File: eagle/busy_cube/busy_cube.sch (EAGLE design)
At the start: 6 parts

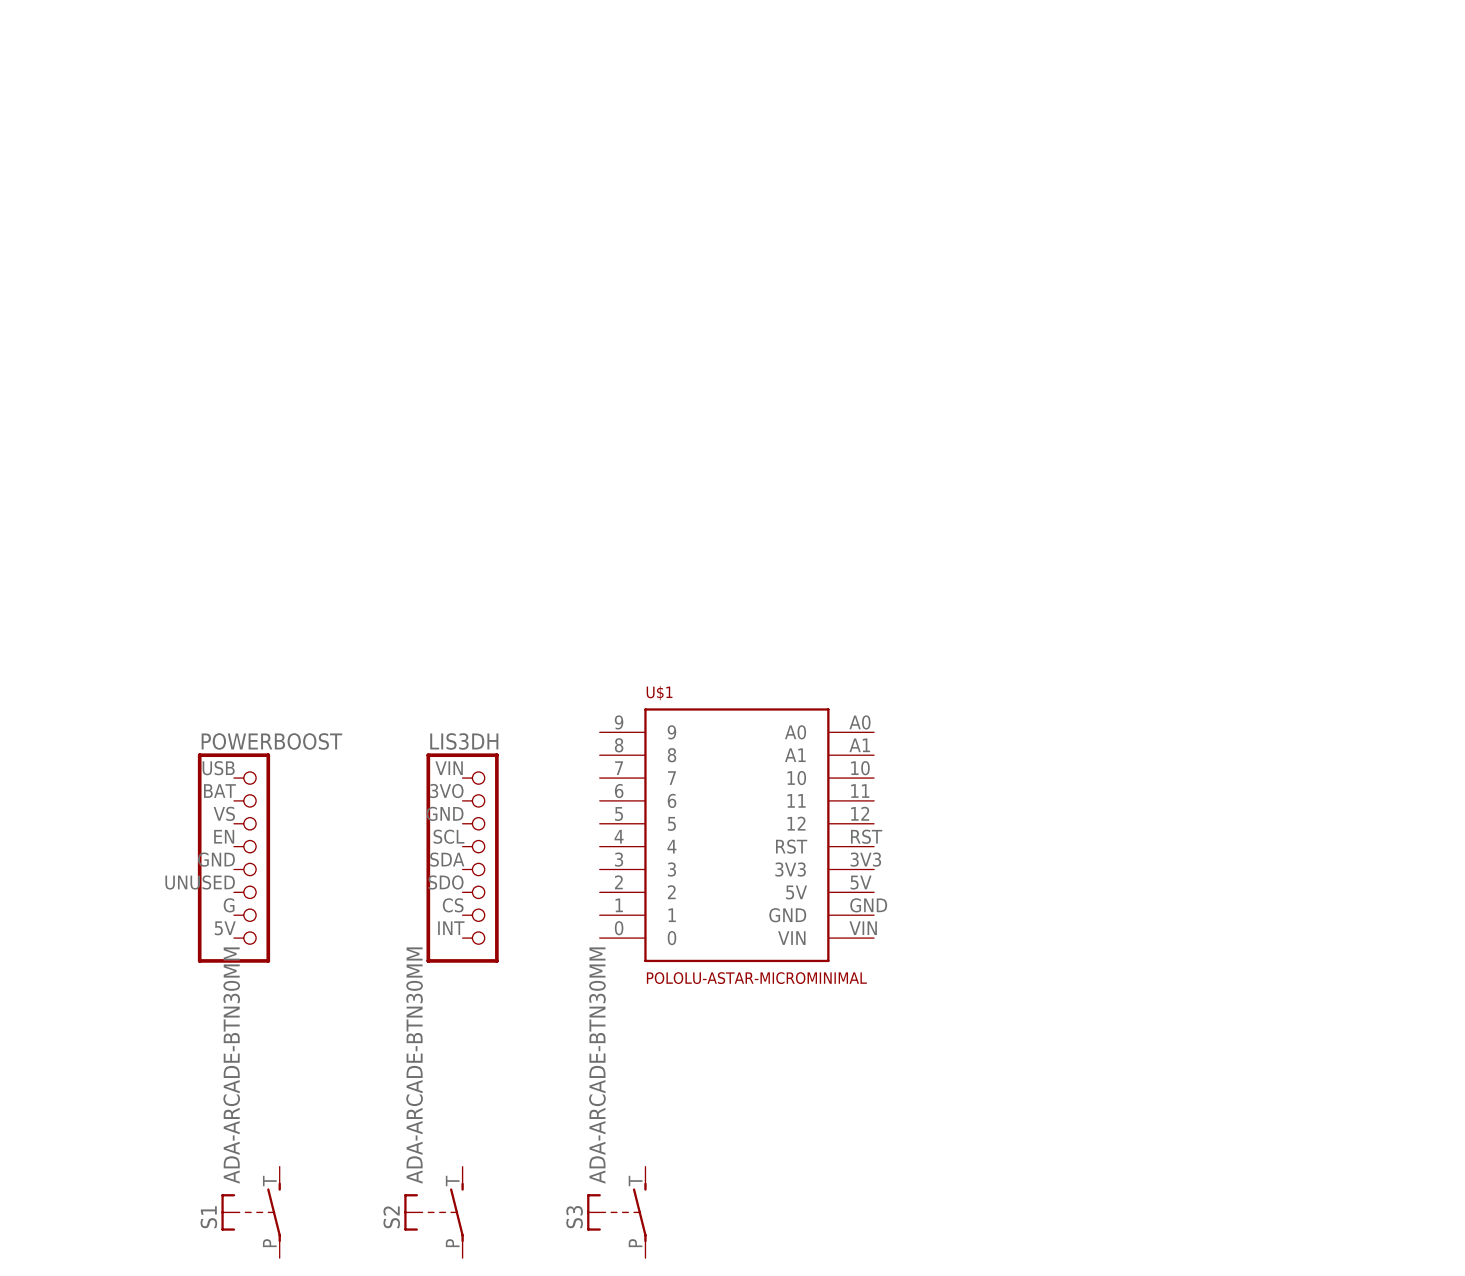
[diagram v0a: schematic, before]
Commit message: First attempt for wiring
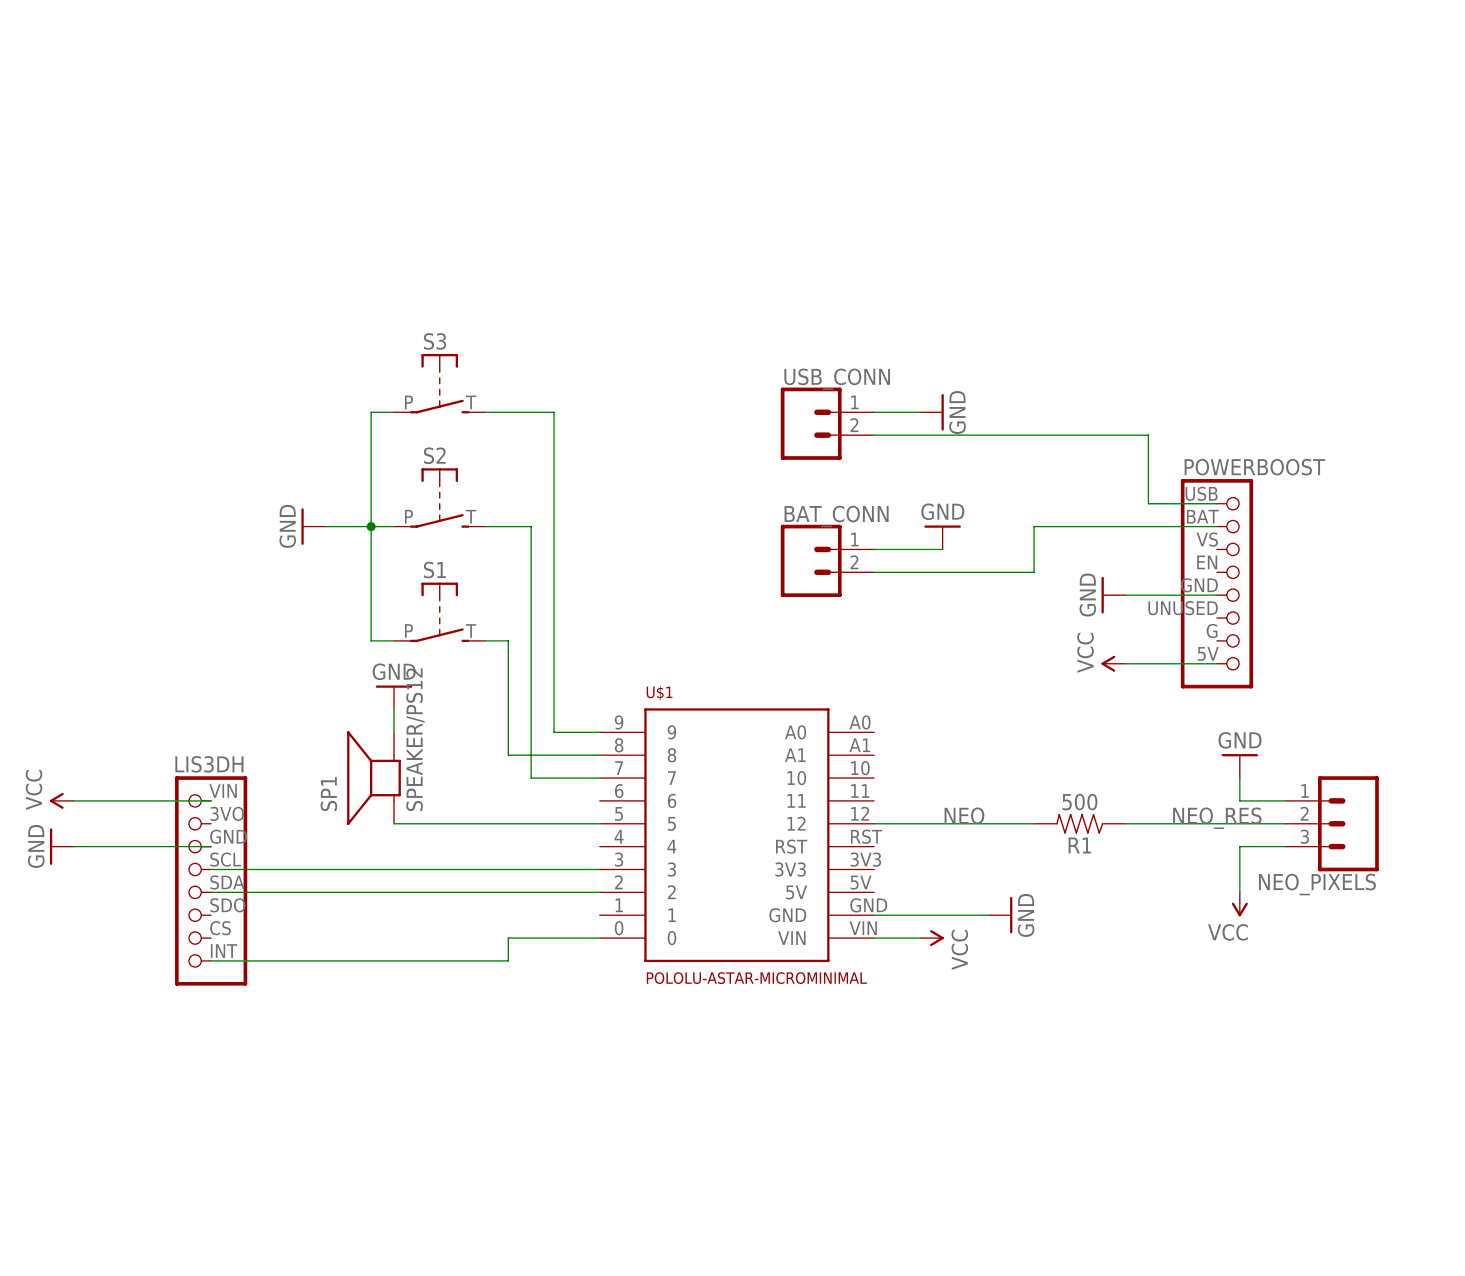
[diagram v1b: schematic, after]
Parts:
- added BAT_CONN, USB_CONN: (no value), busy_cube_lib:CONN_02-JST-2MM-SMT
- added NEO_PIXELS: (no value), busy_cube_lib:CONN_03LONGPADS
- added R1: 500, busy_cube_lib:RESISTORAXIAL-0.3
- added SP1: SPEAKER/PS12, busy_cube_lib:SPEAKER/PS12
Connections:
- new net BAT_IN_VCC: BAT_CONN.1, POWERBOOST.3VO
- new net BTN1: S1.S, U$1.8
- new net BTN2: S2.S, U$1.7
- new net BTN3: S3.S, U$1.9
- new net GND: BAT_CONN.2, LIS3DH.GND, NEO_PIXELS.1, POWERBOOST.SDA, S1.P, S2.P, S3.P, SP1.-, U$1.GND, USB_CONN.2
- new net N$1: LIS3DH.SCL, U$1.3
- new net N$2: LIS3DH.SDA, U$1.2
- new net N$3: LIS3DH.INT, U$1.0
- new net NEO: R1.2, U$1.12
- new net NEO_RES: NEO_PIXELS.2, R1.1
- new net SPKR: SP1.+, U$1.5
- new net USB_IN_VCC: POWERBOOST.VIN, USB_CONN.1
- new net VCC: LIS3DH.VIN, NEO_PIXELS.3, POWERBOOST.INT, U$1.VIN
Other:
- moved on the sheet: LIS3DH, POWERBOOST, S1, S2, S3

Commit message: some more changes
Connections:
- net BTN1: now also U$1.11; no longer U$1.8
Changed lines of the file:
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@@
-</segment>
-</net>
-<net name="BTN1" class="0">
-<segment>
-<pinref part="U$1" gate="G$1" pin="8"/>
-<wire x1="33.02" y1="66.04" x2="22.86" y2="66.04" width="0.1524" layer="91"/>
-<pinref part="S1" gate="G$1" pin="S"/>
-<wire x1="22.86" y1="78.74" x2="20.32" y2="78.74" width="0.1524" layer="91"/>
-<wire x1="22.86" y1="66.04" x2="22.86" y2="78.74" width="0.1524" layer="91"/>
 </segment>
 </net>
@@
 <pinref part="S3" gate="G$1" pin="S"/>
 <wire x1="27.94" y1="104.14" x2="20.32" y2="104.14" width="0.1524" layer="91"/>
+<label x="22.86" y="104.14" size="1.778" layer="95"/>
 </segment>
 </net>
@@
 <pinref part="U$1" gate="G$1" pin="7"/>
 <wire x1="25.4" y1="63.5" x2="33.02" y2="63.5" width="0.1524" layer="91"/>
+<label x="20.32" y="91.44" size="1.778" layer="95"/>
 </segment>
 </net>
@@
 </segment>
 </net>
+<net name="BTN1" class="0">
+<segment>
+<pinref part="S1" gate="G$1" pin="S"/>
+<wire x1="20.32" y1="78.74" x2="68.58" y2="78.74" width="0.1524" layer="91"/>
+<wire x1="68.58" y1="78.74" x2="68.58" y2="60.96" width="0.1524" layer="91"/>
+<pinref part="U$1" gate="G$1" pin="11"/>
+<wire x1="68.58" y1="60.96" x2="63.5" y2="60.96" width="0.1524" layer="91"/>
+<label x="40.64" y="78.74" size="1.778" layer="95"/>
+</segment>
+</net>

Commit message: small changes
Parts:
- removed S3: ADA-ARCADE-BTN30MM, busy_cube_lib:ADA-ARCADE-BTN30MM
- added S0: ADA-ARCADE-BTN30MM, busy_cube_lib:ADA-ARCADE-BTN30MM
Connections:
- removed net BTN3: S3.S, U$1.9
- new net BTN0: S0.S, U$1.11
- net BTN1: now also U$1.7; no longer U$1.11
- net BTN2: now also U$1.9; no longer U$1.7
- net GND: now also S0.P; no longer S3.P
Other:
- moved on the sheet: S1, S2
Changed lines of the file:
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@@
 <part name="POWERBOOST" library="busy_cube_lib" deviceset="ADA-POWERBOOST-1000C" device="PADS-ONLY"/>
 <part name="LIS3DH" library="busy_cube_lib" deviceset="ADA-LIS3DH" device="PADS_ONLY"/>
+<part name="S0" library="busy_cube_lib" deviceset="ADA-ARCADE-BTN" device="30MM"/>
 <part name="S1" library="busy_cube_lib" deviceset="ADA-ARCADE-BTN" device="30MM"/>
 <part name="S2" library="busy_cube_lib" deviceset="ADA-ARCADE-BTN" device="30MM"/>
-<part name="S3" library="busy_cube_lib" deviceset="ADA-ARCADE-BTN" device="30MM"/>
 <part name="USB_CONN" library="busy_cube_lib" deviceset="CONN_02" device="-JST-2MM-SMT"/>
 <part name="BAT_CONN" library="busy_cube_lib" deviceset="CONN_02" device="-JST-2MM-SMT"/>
@@
 <instance part="POWERBOOST" gate="G$1" x="104.14" y="86.36"/>
 <instance part="LIS3DH" gate="G$1" x="-12.7" y="53.34" rot="MR0"/>
-<instance part="S1" gate="G$1" x="15.24" y="81.28" smashed="yes" rot="R270">
+<instance part="S0" gate="G$1" x="15.24" y="81.28" smashed="yes" rot="R270">
 <attribute name="NAME" x="13.335" y="85.725" size="1.778" layer="95"/>
 </instance>
-<instance part="S2" gate="G$1" x="15.24" y="93.98" smashed="yes" rot="R270">
+<instance part="S1" gate="G$1" x="15.24" y="93.98" smashed="yes" rot="R270">
 <attribute name="NAME" x="13.335" y="98.425" size="1.778" layer="95"/>
 </instance>
-<instance part="S3" gate="G$1" x="15.24" y="106.68" smashed="yes" rot="R270">
+<instance part="S2" gate="G$1" x="15.24" y="106.68" smashed="yes" rot="R270">
 <attribute name="NAME" x="13.335" y="111.125" size="1.778" layer="95"/>
 </instance>
@@
 <wire x1="2.54" y1="91.44" x2="7.62" y2="91.44" width="0.1524" layer="91"/>
 <wire x1="7.62" y1="91.44" x2="7.62" y2="104.14" width="0.1524" layer="91"/>
-<pinref part="S3" gate="G$1" pin="P"/>
+<pinref part="S2" gate="G$1" pin="P"/>
 <wire x1="7.62" y1="104.14" x2="10.16" y2="104.14" width="0.1524" layer="91"/>
-<pinref part="S2" gate="G$1" pin="P"/>
+<pinref part="S1" gate="G$1" pin="P"/>
 <wire x1="7.62" y1="91.44" x2="10.16" y2="91.44" width="0.1524" layer="91"/>
 <junction x="7.62" y="91.44"/>
 <wire x1="7.62" y1="91.44" x2="7.62" y2="78.74" width="0.1524" layer="91"/>
-<pinref part="S1" gate="G$1" pin="P"/>
+<pinref part="S0" gate="G$1" pin="P"/>
 <wire x1="10.16" y1="78.74" x2="7.62" y2="78.74" width="0.1524" layer="91"/>
 </segment>
@@
 </segment>
 </net>
-<net name="BTN3" class="0">
+<net name="BTN2" class="0">
 <segment>
 <pinref part="U$1" gate="G$1" pin="9"/>
 <wire x1="33.02" y1="68.58" x2="27.94" y2="68.58" width="0.1524" layer="91"/>
 <wire x1="27.94" y1="68.58" x2="27.94" y2="104.14" width="0.1524" layer="91"/>
-<pinref part="S3" gate="G$1" pin="S"/>
+<pinref part="S2" gate="G$1" pin="S"/>
 <wire x1="27.94" y1="104.14" x2="20.32" y2="104.14" width="0.1524" layer="91"/>
 <label x="22.86" y="104.14" size="1.778" layer="95"/>
@@
 </segment>
 </net>
-<net name="BTN2" class="0">
-<segment>
-<pinref part="S2" gate="G$1" pin="S"/>
+<net name="BTN1" class="0">
+<segment>
+<pinref part="S1" gate="G$1" pin="S"/>
 <wire x1="20.32" y1="91.44" x2="25.4" y2="91.44" width="0.1524" layer="91"/>
 <wire x1="25.4" y1="91.44" x2="25.4" y2="63.5" width="0.1524" layer="91"/>
@@
 </segment>
 </net>
-<net name="BTN1" class="0">
-<segment>
-<pinref part="S1" gate="G$1" pin="S"/>
+<net name="BTN0" class="0">
+<segment>
+<pinref part="S0" gate="G$1" pin="S"/>
 <wire x1="20.32" y1="78.74" x2="68.58" y2="78.74" width="0.1524" layer="91"/>
 <wire x1="68.58" y1="78.74" x2="68.58" y2="60.96" width="0.1524" layer="91"/>

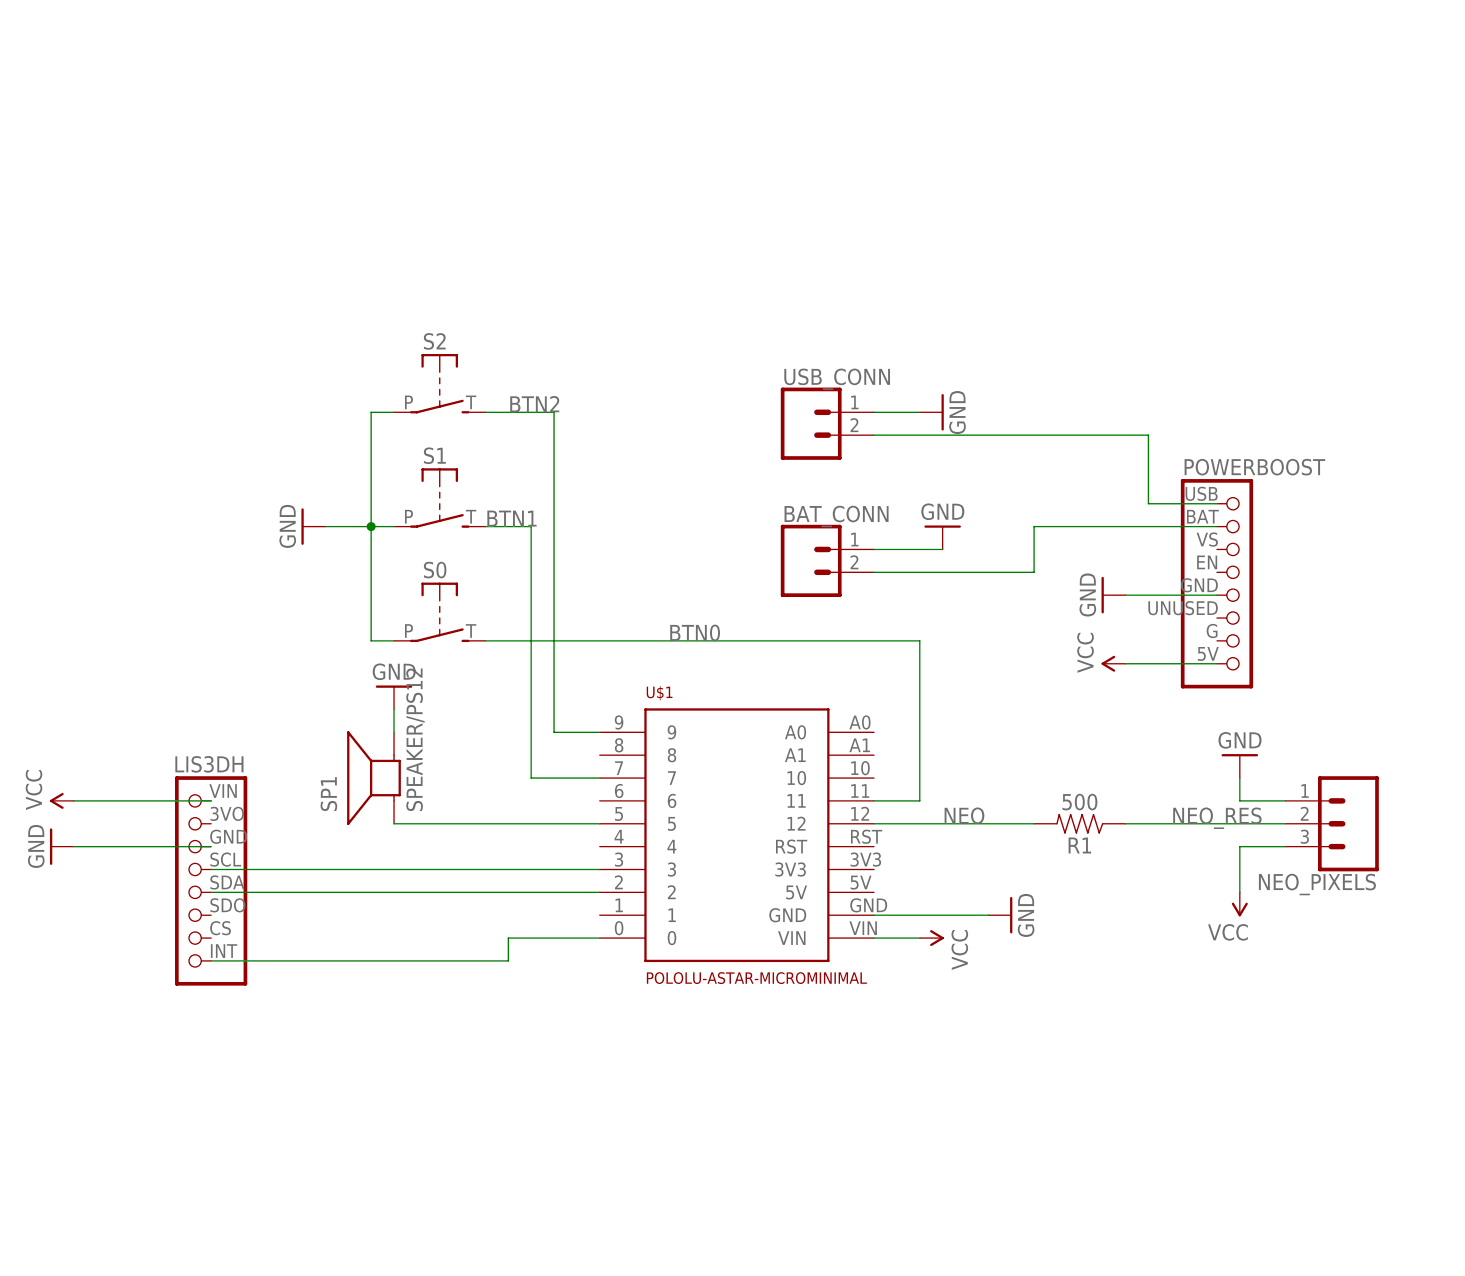
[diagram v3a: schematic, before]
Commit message: Major changes since I need to switch to SPI with the accelerometer
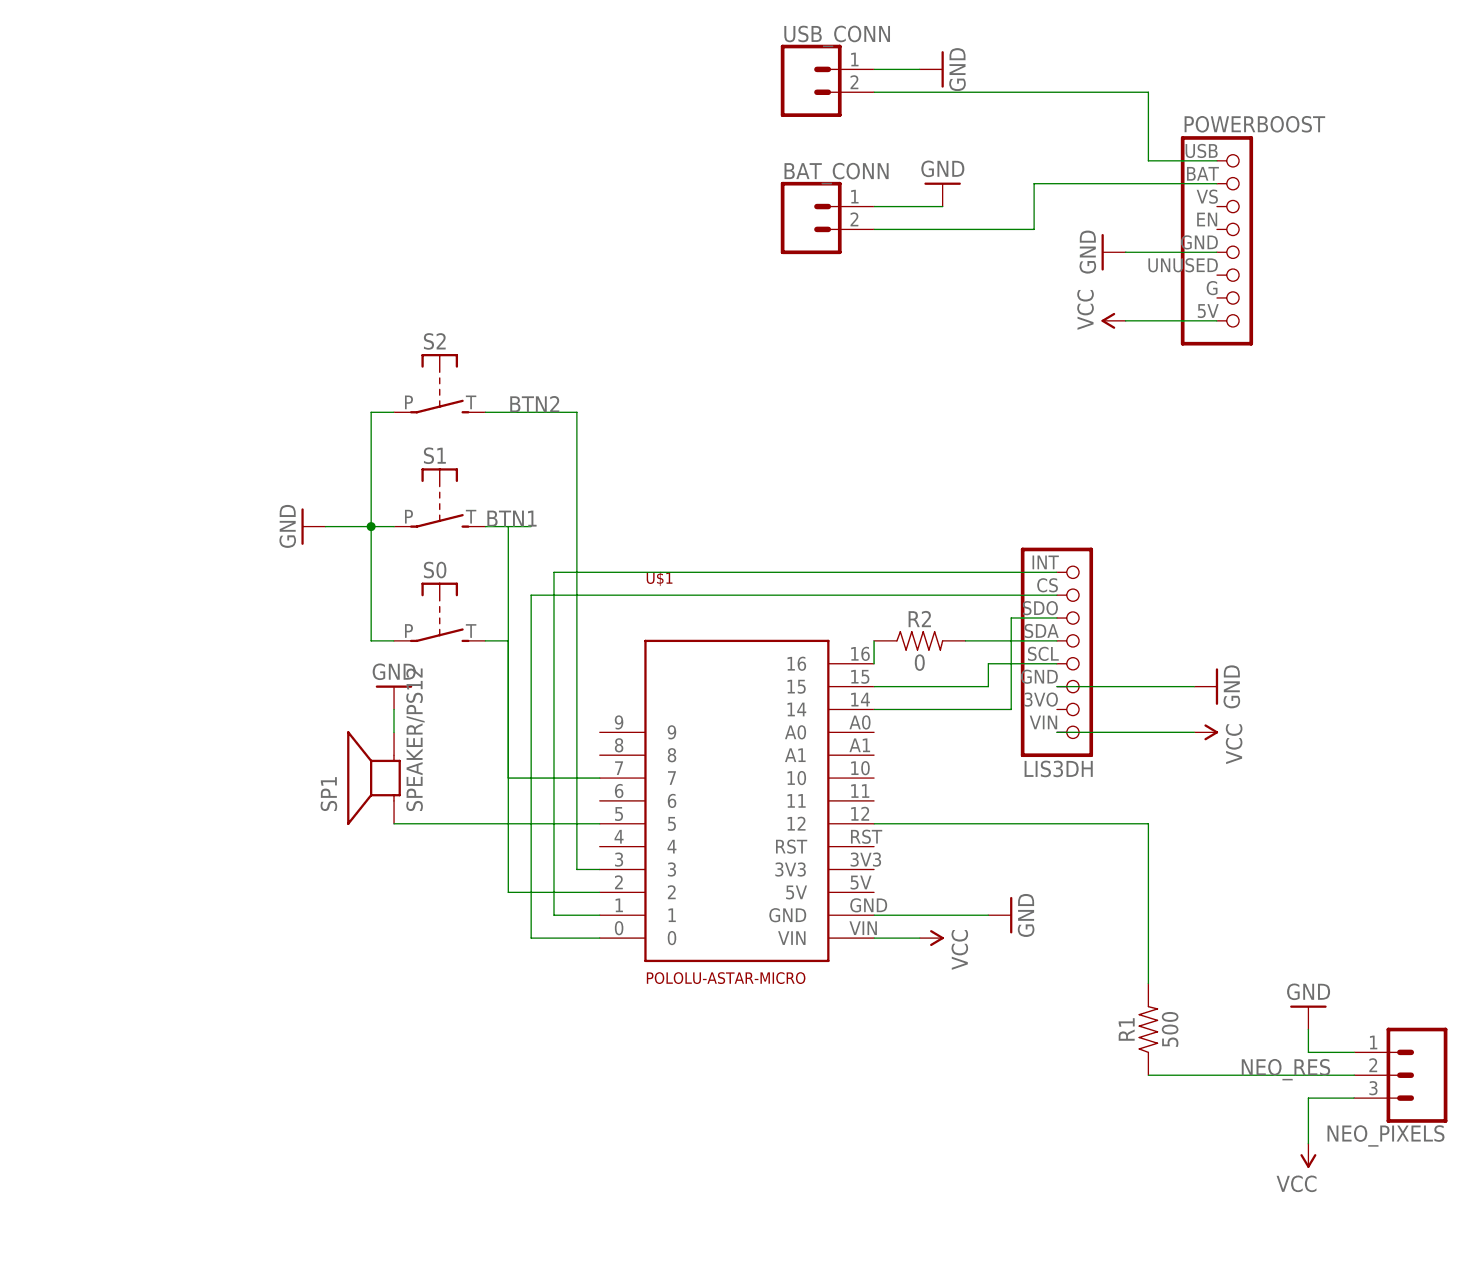
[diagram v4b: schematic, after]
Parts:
- added R2: 0, busy_cube_lib:RESISTOR1206
- U$1: value POLOLU-ASTAR-MICROMINIMAL -> POLOLU-ASTAR-MICRO; device busy_cube_lib:POLOLU-ASTAR-MICROMINIMAL -> busy_cube_lib:POLOLU-ASTAR-MICRO
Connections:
- net NEO renamed N$2
- removed net BTN0: S0.S, U$1.11
- removed net N$2 (its old number): LIS3DH.SDA, U$1.2
- new net N$4: LIS3DH.SDO, U$1.14
- new net N$5: R2.1, U$1.16
- new net N$6: LIS3DH.SCL, U$1.15
- new net N$7: S0.S, U$1.7
- new net N$8: LIS3DH.SDA, R2.2
- net BTN1: now also U$1.2; no longer U$1.7
- net BTN2: now also U$1.3; no longer U$1.9
- net N$1: now also LIS3DH.INT, U$1.1; no longer LIS3DH.SCL, U$1.3
- net N$3: now also LIS3DH.CS; no longer LIS3DH.INT
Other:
- moved on the sheet: BAT_CONN, LIS3DH, NEO_PIXELS, POWERBOOST, R1, USB_CONN
